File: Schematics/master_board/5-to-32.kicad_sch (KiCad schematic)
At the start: 3 parts

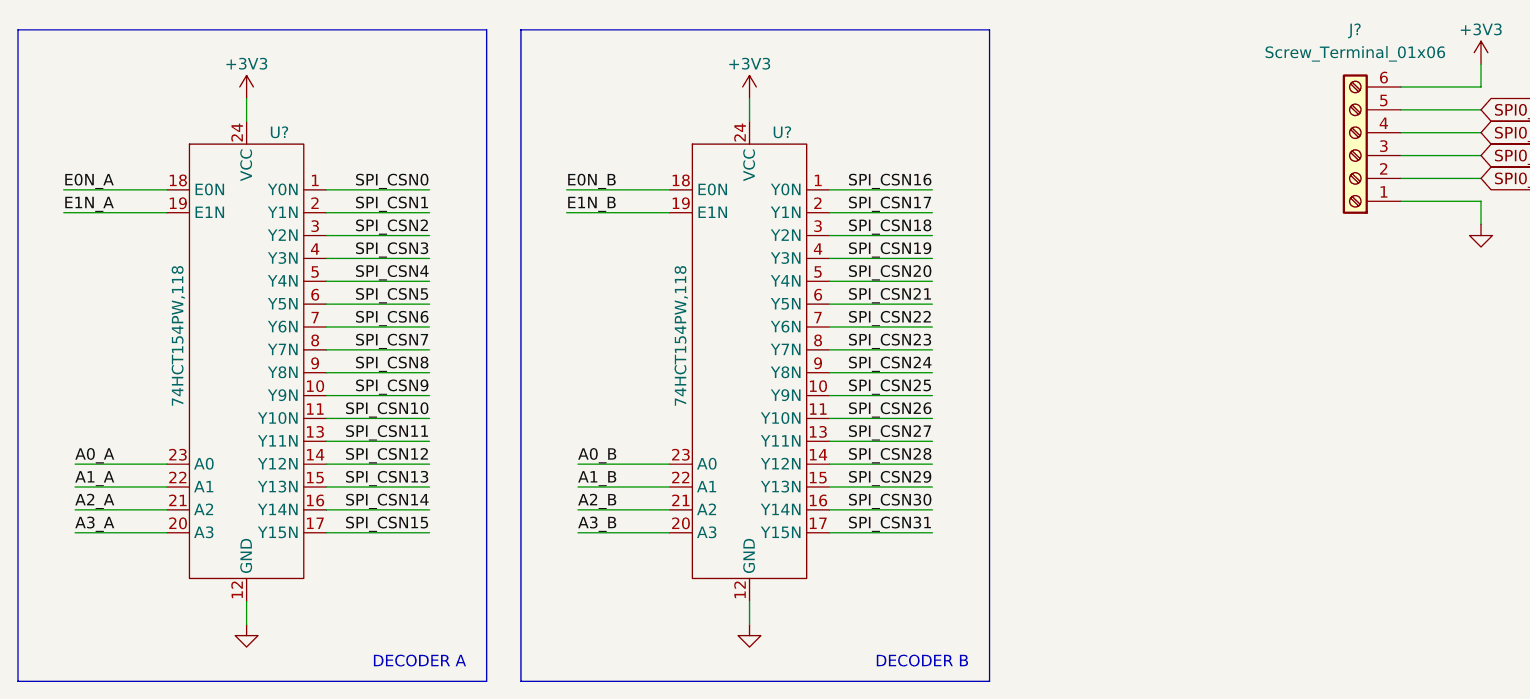
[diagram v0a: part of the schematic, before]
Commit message: Add haptic feedback to master board
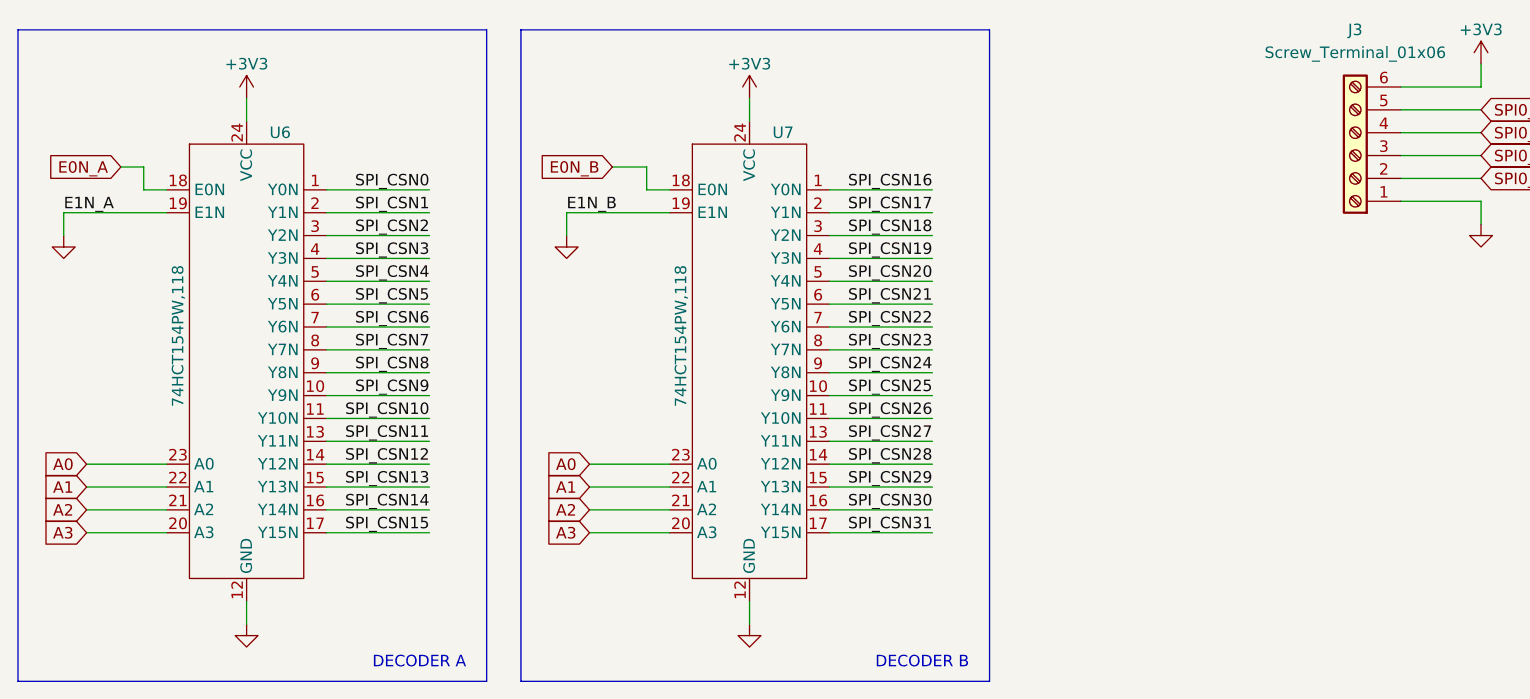
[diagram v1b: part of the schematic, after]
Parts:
- gave numbers to parts that had none: 3
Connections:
- net A0_B is gone; now on net A0: U7.23 (A0)
- net A1_B is gone; now on net A1: U7.22 (A1)
- net A2_B is gone; now on net A2: U7.21 (A2)
- net A3_B is gone; now on net A3: U7.20 (A3)
- net E1N_A is gone; now on net GND: U6.19 (E1N)
- net E1N_B is gone; now on net GND: U7.19 (E1N)
- net A0_A renamed A0
- net A1_A renamed A1
- net A2_A renamed A2
- net A3_A renamed A3

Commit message: Assigned master board footprints
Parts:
- U6, U7: footprint (none) -> Package_SO:TSSOP-24_4.4x5mm_P0.4mm
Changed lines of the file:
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@@
       (effects (font (size 1.27 1.27)) (justify left))
     )
-    (property "Footprint" "" (id 2) (at 63.5 53.34 0)
+    (property "Footprint" "Package_SO:TSSOP-24_4.4x5mm_P0.4mm" (id 2) (at 63.5 53.34 0)
       (effects (font (size 1.27 1.27)) hide)
     )
@@
       (effects (font (size 1.27 1.27)) (justify left))
     )
-    (property "Footprint" "" (id 2) (at 119.38 53.34 0)
+    (property "Footprint" "Package_SO:TSSOP-24_4.4x5mm_P0.4mm" (id 2) (at 119.38 53.34 0)
       (effects (font (size 1.27 1.27)) hide)
     )

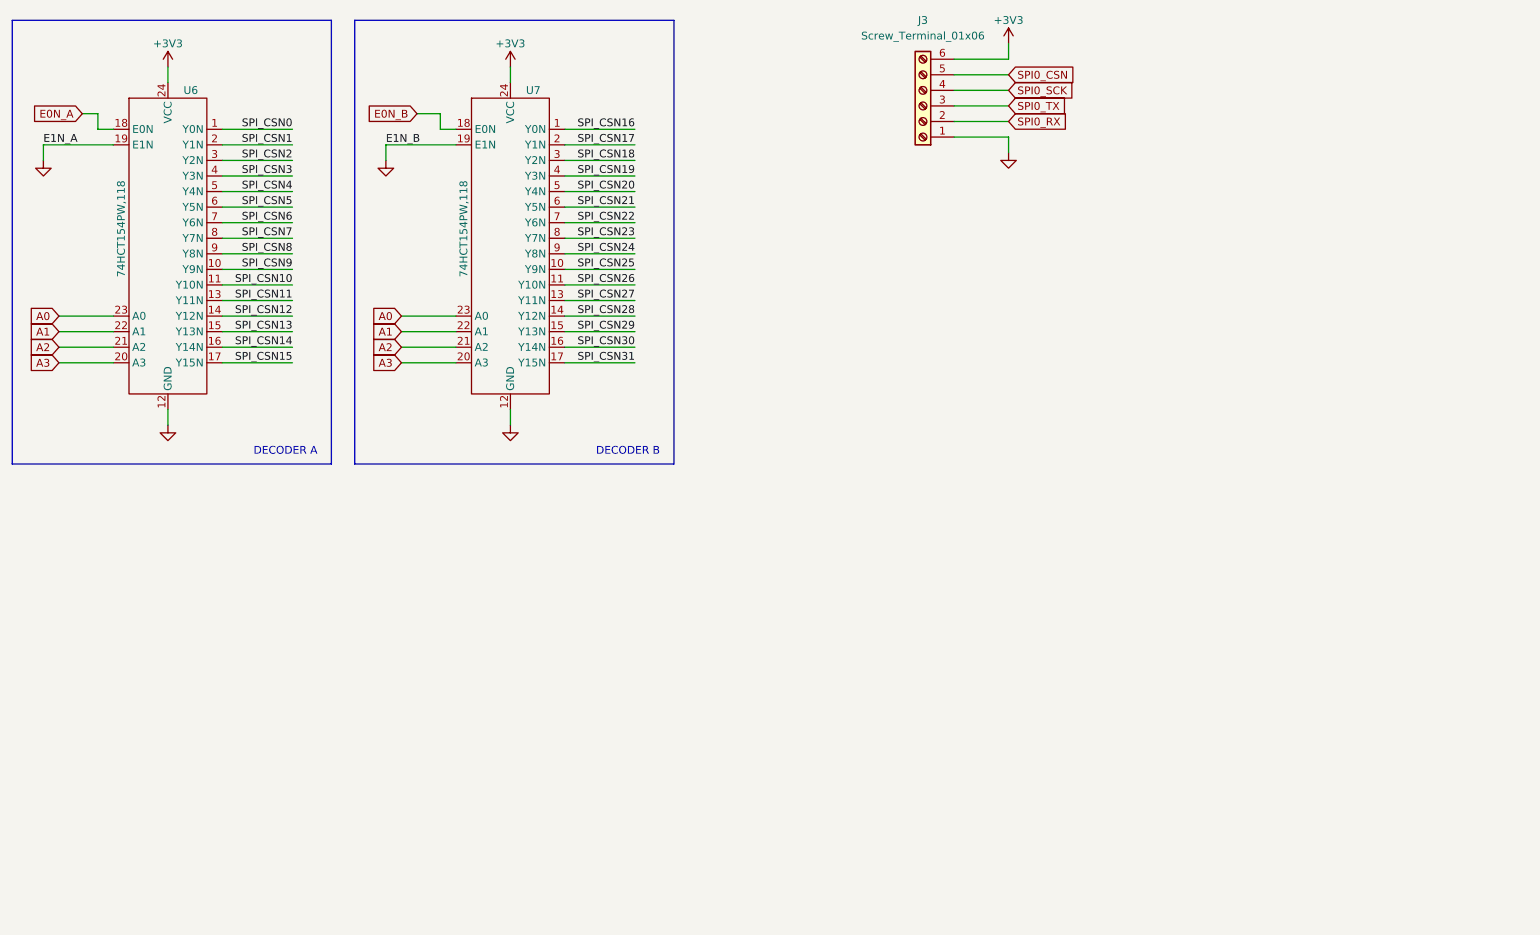
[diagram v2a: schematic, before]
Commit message: Master board connectors and ERC
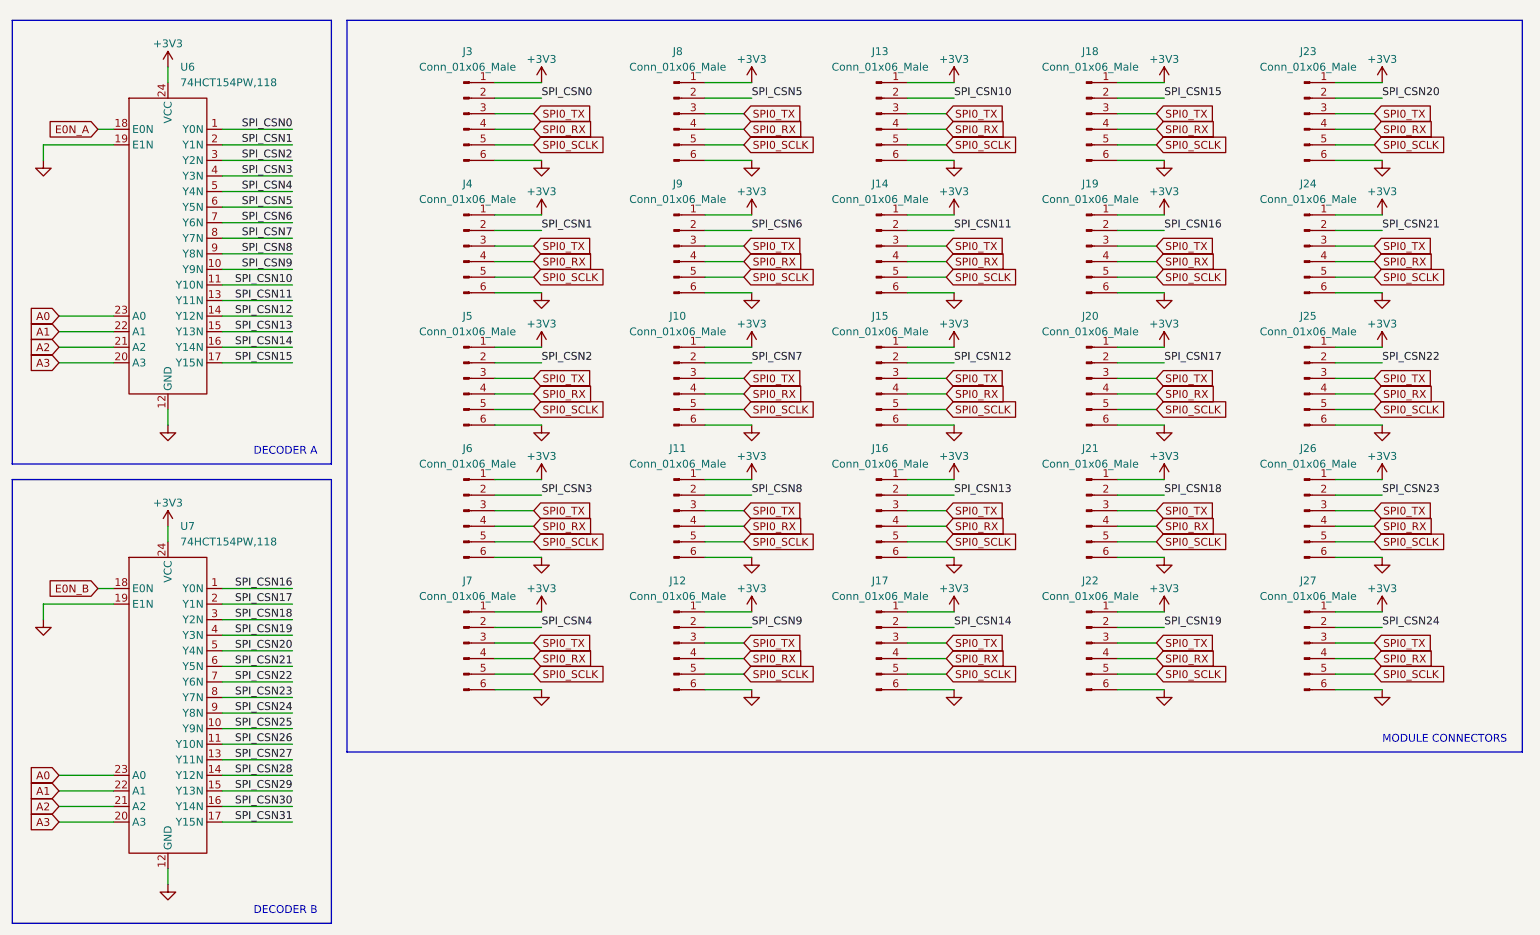
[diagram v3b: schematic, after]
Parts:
- removed J3: Screw_Terminal_01x06, symbol Connector:Screw_Terminal_01x06
- removed U6, U7: 74HCT154PW,118, Package_SO:TSSOP-24_4.4x5mm_P0.4mm, symbol Merrick_Symbols_KiCad6:74HCT154PW,118
- added J10, J11, J12, J13, J14, J15, J16, J17, J18, J19, J20, J21, J22, J23, J24, J25, J26, J27, J3, J4, J5, J6, J7, J8, J9: Conn_01x06_Male, symbol Connector:Conn_01x06_Male
- added U6, U7: 74HCT154PW,118, Package_SO:TSSOP-24_4.4x5mm_P0.4mm, symbol prototroller_symbols:74HCT154PW,118
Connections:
- net +3V3: now also J10.1 (Pin_1), J11.1 (Pin_1), J12.1 (Pin_1), J13.1 (Pin_1), J14.1 (Pin_1), J15.1 (Pin_1), J16.1 (Pin_1), J17.1 (Pin_1), J18.1 (Pin_1), J19.1 (Pin_1), J20.1 (Pin_1), J21.1 (Pin_1), J22.1 (Pin_1), J23.1 (Pin_1), J24.1 (Pin_1), J25.1 (Pin_1), J26.1 (Pin_1), J27.1 (Pin_1), J3.1 (Pin_1), J4.1 (Pin_1), J5.1 (Pin_1), J6.1 (Pin_1), J7.1 (Pin_1), J8.1 (Pin_1), J9.1 (Pin_1), U6.24 (VCC), U7.24 (VCC)
- net A0: now also U6.23 (A0), U7.23 (A0)
- net A1: now also U6.22 (A1), U7.22 (A1)
- net A2: now also U6.21 (A2), U7.21 (A2)
- net A3: now also U6.20 (A3), U7.20 (A3)
- net E0N_A: now also U6.18 (E0N)
- net E0N_B: now also U7.18 (E0N)
- net GND: now also J10.6 (Pin_6), J11.6 (Pin_6), J12.6 (Pin_6), J13.6 (Pin_6), J14.6 (Pin_6), J15.6 (Pin_6), J16.6 (Pin_6), J17.6 (Pin_6), J18.6 (Pin_6), J19.6 (Pin_6), J20.6 (Pin_6), J21.6 (Pin_6), J22.6 (Pin_6), J23.6 (Pin_6), J24.6 (Pin_6), J25.6 (Pin_6), J26.6 (Pin_6), J27.6 (Pin_6), J3.6 (Pin_6), J4.6 (Pin_6), J5.6 (Pin_6), J6.6 (Pin_6), J7.6 (Pin_6), J8.6 (Pin_6), J9.6 (Pin_6), U6.12 (GND), U6.19 (E1N), U7.12 (GND), U7.19 (E1N)
- net SPI0_RX: now also J10.4 (Pin_4), J11.4 (Pin_4), J12.4 (Pin_4), J13.4 (Pin_4), J14.4 (Pin_4), J15.4 (Pin_4), J16.4 (Pin_4), J17.4 (Pin_4), J18.4 (Pin_4), J19.4 (Pin_4), J20.4 (Pin_4), J21.4 (Pin_4), J22.4 (Pin_4), J23.4 (Pin_4), J24.4 (Pin_4), J25.4 (Pin_4), J26.4 (Pin_4), J27.4 (Pin_4), J3.4 (Pin_4), J4.4 (Pin_4), J5.4 (Pin_4), J6.4 (Pin_4), J7.4 (Pin_4), J8.4 (Pin_4), J9.4 (Pin_4)
- net SPI0_TX: now also J10.3 (Pin_3), J11.3 (Pin_3), J12.3 (Pin_3), J13.3 (Pin_3), J14.3 (Pin_3), J15.3 (Pin_3), J16.3 (Pin_3), J17.3 (Pin_3), J18.3 (Pin_3), J19.3 (Pin_3), J20.3 (Pin_3), J21.3 (Pin_3), J22.3 (Pin_3), J23.3 (Pin_3), J24.3 (Pin_3), J25.3 (Pin_3), J26.3 (Pin_3), J27.3 (Pin_3), J3.3 (Pin_3), J4.3 (Pin_3), J5.3 (Pin_3), J6.3 (Pin_3), J7.3 (Pin_3), J8.3 (Pin_3), J9.3 (Pin_3)
- net SPI_CSN0: now also J3.2 (Pin_2), U6.1 (Y0N)
- net SPI_CSN1: now also J4.2 (Pin_2), U6.2 (Y1N)
- net SPI_CSN10: now also J13.2 (Pin_2), U6.11 (Y10N)
- net SPI_CSN11: now also J14.2 (Pin_2), U6.13 (Y11N)
- net SPI_CSN12: now also J15.2 (Pin_2), U6.14 (Y12N)
- net SPI_CSN13: now also J16.2 (Pin_2), U6.15 (Y13N)
- net SPI_CSN14: now also J17.2 (Pin_2), U6.16 (Y14N)
- net SPI_CSN15: now also J18.2 (Pin_2), U6.17 (Y15N)
- net SPI_CSN16: now also J19.2 (Pin_2), U7.1 (Y0N)
- net SPI_CSN17: now also J20.2 (Pin_2), U7.2 (Y1N)
- net SPI_CSN18: now also J21.2 (Pin_2), U7.3 (Y2N)
- net SPI_CSN19: now also J22.2 (Pin_2), U7.4 (Y3N)
- net SPI_CSN2: now also J5.2 (Pin_2), U6.3 (Y2N)
- net SPI_CSN20: now also J23.2 (Pin_2), U7.5 (Y4N)
- net SPI_CSN21: now also J24.2 (Pin_2), U7.6 (Y5N)
- net SPI_CSN22: now also J25.2 (Pin_2), U7.7 (Y6N)
- net SPI_CSN23: now also J26.2 (Pin_2), U7.8 (Y7N)
- net SPI_CSN24: now also J27.2 (Pin_2), U7.9 (Y8N)
- net SPI_CSN25: now also U7.10 (Y9N)
- net SPI_CSN26: now also U7.11 (Y10N)
- net SPI_CSN27: now also U7.13 (Y11N)
- net SPI_CSN28: now also U7.14 (Y12N)
- net SPI_CSN29: now also U7.15 (Y13N)
- net SPI_CSN3: now also J6.2 (Pin_2), U6.4 (Y3N)
- net SPI_CSN30: now also U7.16 (Y14N)
- net SPI_CSN31: now also U7.17 (Y15N)
- net SPI_CSN4: now also J7.2 (Pin_2), U6.5 (Y4N)
- net SPI_CSN5: now also J8.2 (Pin_2), U6.6 (Y5N)
- net SPI_CSN6: now also J9.2 (Pin_2), U6.7 (Y6N)
- net SPI_CSN7: now also J10.2 (Pin_2), U6.8 (Y7N)
- net SPI_CSN8: now also J11.2 (Pin_2), U6.9 (Y8N)
- net SPI_CSN9: now also J12.2 (Pin_2), U6.10 (Y9N)
- new net SPI0_SCLK: J10.5 (Pin_5), J11.5 (Pin_5), J12.5 (Pin_5), J13.5 (Pin_5), J14.5 (Pin_5), J15.5 (Pin_5), J16.5 (Pin_5), J17.5 (Pin_5), J18.5 (Pin_5), J19.5 (Pin_5), J20.5 (Pin_5), J21.5 (Pin_5), J22.5 (Pin_5), J23.5 (Pin_5), J24.5 (Pin_5), J25.5 (Pin_5), J26.5 (Pin_5), J27.5 (Pin_5), J3.5 (Pin_5), J4.5 (Pin_5), J5.5 (Pin_5), J6.5 (Pin_5), J7.5 (Pin_5), J8.5 (Pin_5), J9.5 (Pin_5)
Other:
- note added: "MODULE CONNECTORS"

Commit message: Update footprints
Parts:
- removed J12, J17, J22, J27, J7: Conn_01x06_Male, symbol Connector:Conn_01x06_Male
- J10: renamed from J6; footprint (none) -> prototroller_footprints:Mag_Pogo_6P_P2.2mm_Female
- J11: renamed from J8; footprint (none) -> prototroller_footprints:Mag_Pogo_6P_P2.2mm_Female
- J12: renamed from J9; footprint (none) -> prototroller_footprints:Mag_Pogo_6P_P2.2mm_Female
- J13: renamed from J10; footprint (none) -> prototroller_footprints:Mag_Pogo_6P_P2.2mm_Female
- J14: renamed from J11; footprint (none) -> prototroller_footprints:Mag_Pogo_6P_P2.2mm_Female
- J15: renamed from J13; footprint (none) -> prototroller_footprints:Mag_Pogo_6P_P2.2mm_Female
- J16: renamed from J14; footprint (none) -> prototroller_footprints:Mag_Pogo_6P_P2.2mm_Female
- J17: renamed from J15; footprint (none) -> prototroller_footprints:Mag_Pogo_6P_P2.2mm_Female
- J18: renamed from J16; footprint (none) -> prototroller_footprints:Mag_Pogo_6P_P2.2mm_Female
- J19: renamed from J18; footprint (none) -> prototroller_footprints:Mag_Pogo_6P_P2.2mm_Female
- J20: renamed from J19; footprint (none) -> prototroller_footprints:Mag_Pogo_6P_P2.2mm_Female
- J21: renamed from J20; footprint (none) -> prototroller_footprints:Mag_Pogo_6P_P2.2mm_Female
- J22: renamed from J21; footprint (none) -> prototroller_footprints:Mag_Pogo_6P_P2.2mm_Female
- J23, J24, J25, J26: footprint (none) -> prototroller_footprints:Mag_Pogo_6P_P2.2mm_Female
- J7: renamed from J3; footprint (none) -> prototroller_footprints:Mag_Pogo_6P_P2.2mm_Female
- J8: renamed from J4; footprint (none) -> prototroller_footprints:Mag_Pogo_6P_P2.2mm_Female
- J9: renamed from J5; footprint (none) -> prototroller_footprints:Mag_Pogo_6P_P2.2mm_Female
- renumbered U6 to U4, U7 to U5
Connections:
- net SPI_CSN10: now also J17.2 (Pin_2); no longer J15.2 (Pin_2)
- net SPI_CSN11: now also J18.2 (Pin_2); no longer J16.2 (Pin_2)
- net SPI_CSN12: now also J19.2 (Pin_2); no longer J17.2 (Pin_2)
- net SPI_CSN13: now also J20.2 (Pin_2); no longer J18.2 (Pin_2)
- net SPI_CSN14: now also J21.2 (Pin_2)
- net SPI_CSN15: now also J22.2 (Pin_2); no longer J19.2 (Pin_2)
- net SPI_CSN16: now also J23.2 (Pin_2); no longer J20.2 (Pin_2)
- net SPI_CSN17: now also J24.2 (Pin_2); no longer J21.2 (Pin_2)
- net SPI_CSN18: now also J25.2 (Pin_2); no longer J22.2 (Pin_2)
- net SPI_CSN19: now also J26.2 (Pin_2)
- net SPI_CSN20: no longer J23.2 (Pin_2)
- net SPI_CSN21: no longer J24.2 (Pin_2)
- net SPI_CSN22: no longer J25.2 (Pin_2)
- net SPI_CSN23: no longer J26.2 (Pin_2)
- net SPI_CSN4: now also J11.2 (Pin_2)
- net SPI_CSN5: now also J12.2 (Pin_2); no longer J11.2 (Pin_2)
- net SPI_CSN6: now also J13.2 (Pin_2); no longer J12.2 (Pin_2)
- net SPI_CSN7: now also J14.2 (Pin_2); no longer J13.2 (Pin_2)
- net SPI_CSN8: now also J15.2 (Pin_2); no longer J14.2 (Pin_2)
- net SPI_CSN9: now also J16.2 (Pin_2)
- no-connect marks 0 -> 12
